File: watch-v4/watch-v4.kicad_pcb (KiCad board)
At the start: 4 copper layers, 35 x 35 mm, 35 parts, among them J1 CONN_10, P1 array connection, Q1 MOSFET_P, SW1 SPST, SW2 SPST, SW3 SPST, U1 IC_MCP73831, U2 MAX1722, U3 DS3231, U4 LSM9DS0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

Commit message: up to version 5.2
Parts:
- removed P1: array connection, watch-v4:Pin_Header_Straight_1x02
- added R4: 10kΩ, Resistors_SMD:R_0603, F.Cu at (159.3, 114.7)
- added R7: 10kΩ, Resistors_SMD:R_0603, F.Cu at (173.1, 114.2)
- added R8: 10kΩ, Resistors_SMD:R_0603, F.Cu at (176.0, 114.2)
- SW1, SW2, SW3: footprint watch-v4:panasonic-evpav-switch -> watch-v4:SW_Tactile_SPST_Angled_no_anchors
- moved C8 31.9 mm to (162.3, 113.1)
- moved SW3 31.0 mm to (183.6, 114.2), turned to 180 degrees
- moved U6 30.4 mm to (176.9, 112.2)
- moved ANT1 30.1 mm to (181.5, 111.9)
- moved XL1 30.1 mm to (177.5, 83.3), turned to 180 degrees
- moved C13 26.9 mm to (169.8, 108.2)
- moved SW1 26.3 mm to (156.3, 114.2), turned to 180 degrees
- moved C14 25.5 mm to (169.8, 110.2)
- moved R1 23.8 mm to (183.8, 85.2), turned to 270 degrees
- moved D2 23.1 mm to (183.7, 82.3), turned to 90 degrees
- moved D1 21.9 mm to (174.7, 91.7)
- moved X1 20.9 mm to (184.1, 109.1), turned to 90 degrees
- moved C1 20.9 mm to (181.5, 88.3)
- moved U5 19.6 mm to (177.5, 107.3), turned to 270 degrees
- moved R3 19.5 mm to (183.8, 87.7)
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- renumbered 12pf1 to 12p
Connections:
- net Net-(SW1-Pad2) renamed /SW1
- net Net-(SW2-Pad2) renamed /SW2
- net Net-(SW3-Pad2) renamed /SW3
- U5 pad 10: DISPLAY_SS -> DISPLAY_SCK
- U5 pad 32: Net-(U5-Pad31) -> Net-(U5-Pad32)
- U5 pad 8: DISPLAY_SCK -> DISPLAY_SS
- U6 pad 1: Net-(U5-Pad31) -> Net-(ANT1-Pad1)
- U6 pad 3: Net-(ANT1-Pad1) -> Net-(U5-Pad32)
- U6 pad 4: Net-(ANT1-Pad1) -> Net-(U5-Pad31)
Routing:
- net VCC: track 133.9 -> 15.3 mm, vias 8 -> 2
- net GND: track 135.4 -> 88.3 mm, vias 5 -> 9
- net SDA: track 54.8 -> 10.4 mm, vias 4 -> 0
- net SCL: track 50.1 -> 8.90 mm, vias 4 -> 0
- net /SW3: track 52.4 -> 15.0 mm, vias 2 -> 0
- net /SW1: track 30.3 -> 0.00 mm, vias 2 -> 0
- net /SW2: track 39.3 -> 9.65 mm, vias 2 -> 0
- net /EXTVCC: track 48.4 -> 25.0 mm, vias 1 -> 0
- net DISPLAY_SS: track 17.0 -> 0.00 mm
- net DISPLAY_MOSI: track 15.6 -> 0.00 mm
- net DISPLAY_SCK: track 14.2 -> 0.00 mm
- net /Regulator_In: track 22.5 -> 31.7 mm, vias 2 -> 3
- net /RX: track 27.4 -> 19.6 mm
- net Net-(R2-Pad1): track 9.80 -> 3.00 mm
- net Net-(C5-Pad1): track 6.57 -> 0.00 mm
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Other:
- outline, holes or cut-outs redrawn
- board text added: "Ourglass Rev 4.6"
- board text removed: "Ourglass Rev 4.5"

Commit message: save v5.2
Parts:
- added U7: NeoPixel, LEDs:Neopixel, B.Cu at (175.4, 96.3)
- moved L1 0.48 mm to (174.1, 100.4), turned to 270 degrees
- moved 12p 0.37 mm to (183.3, 105.5)
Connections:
- U3 pad 3: Net-(U3-Pad3) -> /ClockINT
- U4 pad 13: Net-(U4-Pad13) -> /Accel_INT
- U5 pad 25: Net-(U5-Pad25) -> /Backlight
- U5 pad 47: Net-(U5-Pad47) -> /ClockINT
- U5 pad 48: Net-(U5-Pad48) -> /Accel_INT
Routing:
- net VCC: track 15.3 -> 92.6 mm, vias 2 -> 9
- net GND: track 88.3 -> 148.3 mm, vias 9 -> 16
- net /Accel_INT: track 0.00 -> 30.6 mm, vias 0 -> 2
- net /SW1: track 0.00 -> 29.3 mm
- net SDA: track 10.4 -> 33.9 mm, vias 0 -> 2
- net SCL: track 8.90 -> 31.6 mm, vias 0 -> 2
- net /Backlight: track 0.00 -> 22.1 mm, vias 0 -> 1
- net /ClockINT: track 0.00 -> 21.4 mm, vias 0 -> 2
- net Net-(C6-Pad1): track 0.00 -> 13.8 mm, vias 0 -> 2
- net Net-(C5-Pad1): track 0.00 -> 8.43 mm
- net /SW2: track 9.65 -> 17.7 mm
- net Net-(C5-Pad2): track 0.00 -> 7.42 mm
- net DISPLAY_SCK: track 0.00 -> 5.91 mm
- net DISPLAY_MOSI: track 0.00 -> 5.17 mm
- net /Reset: track 27.5 -> 32.1 mm
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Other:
- board text added: "Ourglass Rev 5.2"
- board text removed: "Ourglass Rev 4.6"

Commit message: further v6 work; incomplete
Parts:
- removed 12p: C9, Capacitors_SMD:C_0603
- removed SW1, SW2, SW3: SPST, watch-v4:SW_Tactile_SPST_Angled_no_anchors
- removed U7: NeoPixel, LEDs:Neopixel
- added 12pf1: C9, Capacitors_SMD:C_0603, F.Cu at (183.4, 105.7)
- added C11: 2n2, Capacitors_SMD:C_0603, F.Cu at (180.1, 112.2)
- added C12: 1u, Capacitors_SMD:C_0603, B.Cu at (180.2, 85.2)
- added C4: 100n, Capacitors_SMD:C_0603, F.Cu at (183.2, 110.8)
- added C9: 47n, Capacitors_SMD:C_0603, F.Cu at (174.2, 114.1)
- added D3: LED, Capacitors_SMD:C_0603, B.Cu at (174.2, 106.5)
- added D4: LED, Capacitors_SMD:C_0603, B.Cu at (174.5, 97.6)
- added D5: LED, Capacitors_SMD:C_0603, B.Cu at (173.9, 87.8)
- added P1: Expansion Header, Socket_Strips:Socket_Strip_Straight_1x12_small, F.Cu at (172.1, 103.8)
- added Q2: BSS138, TO_SOT_Packages_SMD:SOT-23, B.Cu at (178.6, 95.3)
- added R9: 47, Resistors_SMD:R_0603, B.Cu at (173.9, 113.7)
- C1, C2, C5, C6, C7, C8, D1, Q1, R5, R6, U1, U2, U3, U4: moved to B.Cu
- C13: value 0.1uf -> 0u1; moved to B.Cu
- C14: value 0.1uf -> 1nf; moved to B.Cu
- C3: value 4.7uf -> 4u7; moved to B.Cu
- D2: footprint LED-0603 -> Capacitors_SMD:C_0603
- LIPOLY1: footprint watch-v4:Pin_Header_Straight_1x02 -> Socket_Strips:molex_2_pos
- R1: value 47Ω -> 47
- R2, R4: value 10kΩ -> 10k; moved to B.Cu
- R3: value R100kΩ -> 100k; moved to B.Cu
- R7, R8: value 10kΩ -> 10M; moved to B.Cu
- moved R7 33.0 mm to (179.7, 81.8)
- moved R8 31.0 mm to (179.8, 83.5)
- moved U4 28.9 mm to (181.8, 112.2), turned to 90 degrees
- moved R4 27.3 mm to (181.4, 98.7)
- moved C14 21.5 mm to (183.3, 93.5), turned to 0 degrees
- moved R5 20.6 mm to (177.8, 107.6), turned to 270 degrees
- moved U3 19.5 mm to (181.4, 103.7), turned to 0 degrees
- moved R6 18.9 mm to (176.0, 107.5), turned to 270 degrees
- moved C13 18.9 mm to (183.3, 95.1), turned to 0 degrees
- moved C7 18.5 mm to (175.8, 110.5), turned to 90 degrees
- moved C5 16.4 mm to (175.8, 113.6), turned to 270 degrees
- moved C8 15.5 mm to (177.6, 110.5), turned to 90 degrees
- moved C6 15.4 mm to (177.6, 113.6), turned to 270 degrees
- moved L1 13.1 mm to (180.5, 88.9)
- moved R3 11.6 mm to (173.5, 82.4), turned to 90 degrees
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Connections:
- net DISPLAY_MOSI renamed /Display_MOSI
- net DISPLAY_SCK renamed /Display_SCK
- net DISPLAY_SS renamed /Display_SS
- net Net-(12pf1-Pad2) renamed /XC2
- net Net-(C10-Pad1) renamed /XC1
- net Net-(U5-Pad31) renamed /Bal1
- net Net-(U5-Pad32) renamed /Bal2
- C13 pad 2: VCC -> /VCC
- C14 pad 2: VCC -> /VCC
- C7 pad 1: VCC -> /VCC
- C8 pad 1: VCC -> /VCC
- J1 pad 5: VCC -> /VCC
- J1 pad 6: VCC -> /VCC
- J1 pad 7: VCC -> /VCC
- J1 pad 8: VCC -> /VCC
- R4 pad 1: /SW1 -> /VCC
- R4 pad 2: GND -> /ClockINT
- R5 pad 1: SDA -> /SCL
- R5 pad 2: VCC -> /VCC
- R6 pad 1: SCL -> /SDA
- R6 pad 2: VCC -> /VCC
- R7 pad 1: /SW2 -> /VBAT
- R7 pad 2: GND -> /BatterySense
- R8 pad 1: GND -> /BatterySense
- R8 pad 2: /SW3 -> GND
- U2 pad 4: VCC -> /VCC
- U3 pad 2: VCC -> /VCC
- U3 pad 6: VCC -> /VCC
- U3 pad 7: SDA -> /SCL
- U3 pad 8: SCL -> /SDA
- U4 pad 15: VCC -> /VCC
- U4 pad 16: VCC -> /VCC
- U4 pad 17: VCC -> /VCC
- U4 pad 18: VCC -> /VCC
- U4 pad 19: VCC -> /VCC
- U4 pad 20: VCC -> /VCC
- U4 pad 21: SCL -> /SCL
- U4 pad 24: SDA -> /SDA
- U5 pad 1: VCC -> /VCC
- U5 pad 12: VCC -> /VCC
- U5 pad 14: /SW1 -> /EX8
- U5 pad 15: /SW2 -> /EX9
- U5 pad 16: /SW3 -> /EX10
- U5 pad 17: Net-(U5-Pad17) -> /EX11
- U5 pad 18: Net-(U5-Pad18) -> /EX12
- U5 pad 19: Net-(U5-Pad19) -> /EX13
- U5 pad 20: Net-(U5-Pad20) -> /EX14
- U5 pad 21: Net-(U5-Pad21) -> /EX15
- U5 pad 22: Net-(U5-Pad22) -> /BatterySense
- U5 pad 30: Net-(U5-Pad30) -> /VDD_PA
- U5 pad 35: VCC -> /VCC
- U5 pad 36: VCC -> /VCC
- U5 pad 6: SCL -> /SCL
- U5 pad 7: SDA -> /SDA
- U6 pad 5: GND -> /VDD_PA
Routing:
- net GND: track 148.3 -> 0.00 mm, vias 16 -> 0
- net VCC: track 92.6 -> 0.00 mm, vias 9 -> 0
- net SDA: track 33.9 -> 0.00 mm, vias 2 -> 0
- net /Reset: track 32.1 -> 0.00 mm, vias 2 -> 0
- net SCL: track 31.6 -> 0.00 mm, vias 2 -> 0
- net /Accel_INT: track 30.6 -> 0.00 mm, vias 2 -> 0
- net /SW1: track 29.3 -> 0.00 mm
- net /EXTVCC: track 25.0 -> 0.00 mm
- net /Regulator_In: track 28.0 -> 3.61 mm, vias 3 -> 0
- net /VBAT: track 24.0 -> 0.00 mm, vias 1 -> 0
- net /Backlight: track 22.1 -> 0.00 mm, vias 1 -> 0
- net /TX: track 22.0 -> 0.00 mm, vias 2 -> 0
- net /ClockINT: track 21.4 -> 0.00 mm, vias 2 -> 0
- net /RX: track 19.5 -> 0.00 mm, vias 2 -> 0
- net /SW2: track 17.7 -> 0.00 mm
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- removed copper zone on B.Cu, net GND
- removed copper zone on F.Cu, net GND
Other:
- board size 35 x 35 mm -> 13 x 35 mm
- board text added: "Ourglass Rev 6.0"
- board text removed: "Ourglass Rev 5.2"

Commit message: further traces routed, still more work to go
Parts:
- C13: value 0u1 -> 0.1uf
- C3: value 4u7 -> 4.7uf
- R1: value 47 -> 47Ω
- R2: value 10k -> 10kΩ
- R3: value 100k -> R100kΩ
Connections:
- P1 pad 1: /VCC -> GND
- P1 pad 2: GND -> /VCC
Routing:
- net GND: track 0.00 -> 41.1 mm, vias 0 -> 7
- net /EXTVCC: track 0.00 -> 21.5 mm, vias 0 -> 3
- net /Regulator_In: track 3.61 -> 22.8 mm, vias 0 -> 1
- net /VBAT: track 0.00 -> 13.3 mm, vias 0 -> 1
- net Net-(D2-Pad2): track 0.00 -> 3.81 mm
- net /BatterySense: track 0.00 -> 3.58 mm
- net /VCC: track 0.00 -> 3.31 mm
- net Net-(L1-Pad2): track 0.00 -> 2.96 mm, vias 0 -> 1
- net Net-(D2-Pad1): track 0.00 -> 2.10 mm, vias 0 -> 1
- net Net-(R2-Pad1): track 0.00 -> 1.80 mm

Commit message: further traces routed, still more work to go
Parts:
- C10: value 12pf -> 12p
- C5: value .22uf -> u22
- C6: value 4.7uf -> 4u7
- C8: value 0.1uf -> u1
- turned D1 to 180 degrees
- renumbered 12pf1 to 12p
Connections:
- P1 pad 3: /SDA -> /SCL
- P1 pad 4: /SCL -> /SDA
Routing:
- net /EXTVCC: track 21.5 -> 35.4 mm, vias 3 -> 2
- net /Regulator_In: track 22.8 -> 18.0 mm
- net /EX8: track 0.00 -> 4.78 mm
- net GND: track 41.1 -> 45.8 mm
- net /EX15: track 0.00 -> 4.57 mm
- net /EX9: track 0.00 -> 3.95 mm
- net /EX14: track 0.00 -> 3.86 mm
- net /EX13: track 0.00 -> 2.97 mm
- net /EX10: track 0.00 -> 2.89 mm
- net /EX12: track 0.00 -> 2.61 mm
- net /EX11: track 0.00 -> 2.53 mm
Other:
- board text added: "10"
- board text added: "11"
- board text added: "12"
- board text added: "13"
- board text added: "14"
- board text added: "15"
- board text added: "8"
- board text added: "9"
- board text added: "GND"
- board text added: "SCL"
- board text added: "SDA"
- board text added: "VCC"

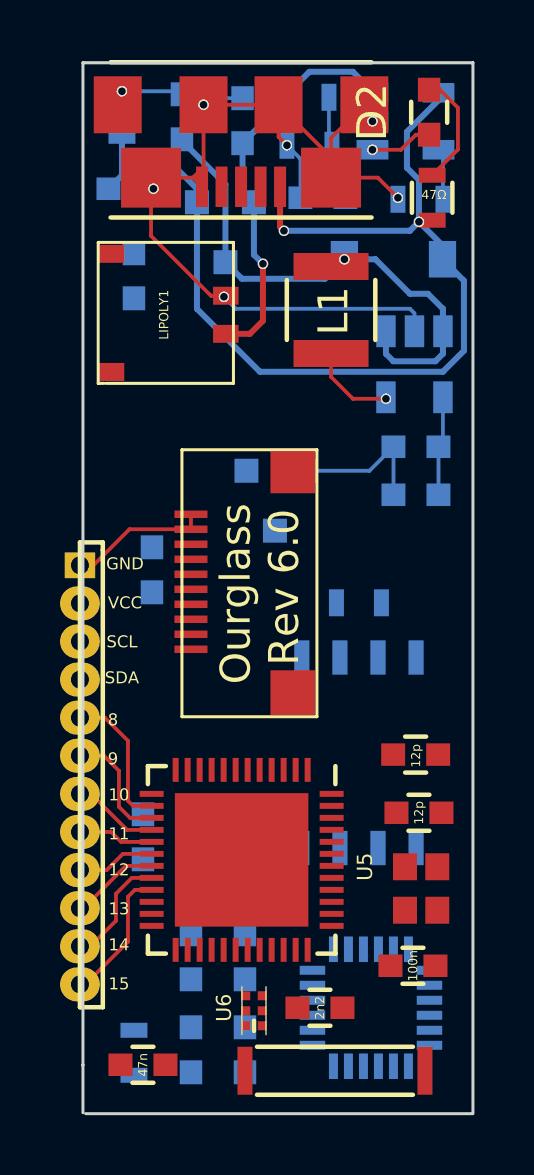
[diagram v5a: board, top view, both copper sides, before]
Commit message: top layer components mostly routed
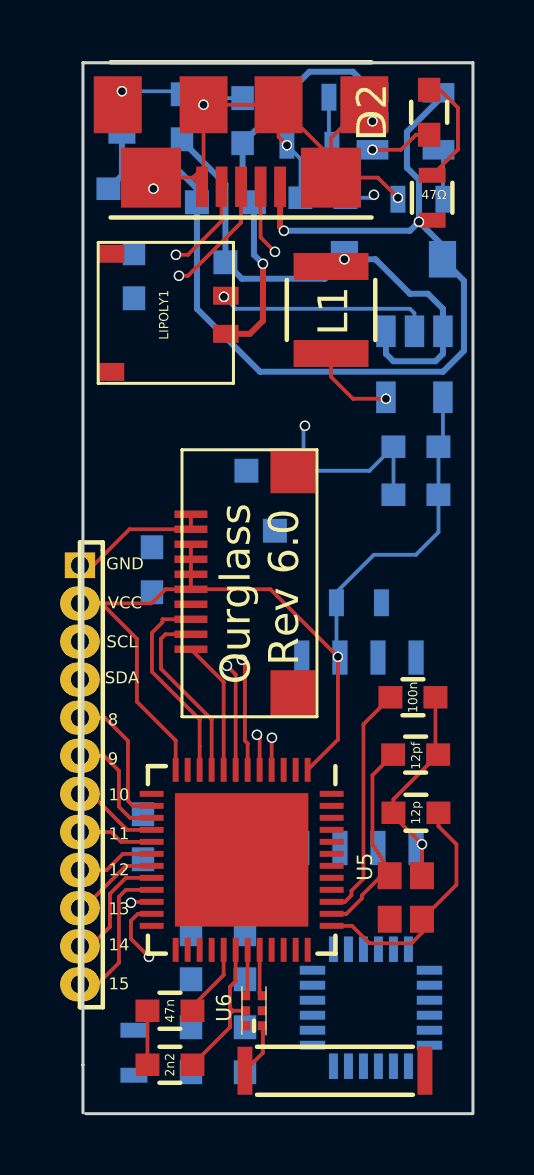
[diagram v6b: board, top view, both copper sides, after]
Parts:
- C10: value 12p -> 12pf
- C5: value u22 -> .22uf
- C6: value 4u7 -> 4.7uf
- C8: value u1 -> 0.1uf
- moved C4 8.95 mm to (183.2, 101.8)
- moved C11 5.35 mm to (175.1, 114.1)
- moved C9 2.01 mm to (175.1, 112.3), turned to 180 degrees
- moved X1 0.59 mm to (183.6, 109.4)
- moved 12p 0.10 mm to (183.3, 105.7)
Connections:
- XL1 pad 2: /RX -> /TX
- XL1 pad 3: /TX -> /RX
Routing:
- net /BatterySense: track 3.58 -> 41.1 mm, vias 0 -> 2
- net /VCC: track 3.31 -> 33.7 mm, vias 0 -> 1
- net /Reset: track 0.00 -> 29.1 mm, vias 0 -> 2
- net /RX: track 0.00 -> 21.6 mm, vias 0 -> 2
- net GND: track 45.8 -> 67.2 mm, vias 7 -> 9
- net /TX: track 0.00 -> 19.7 mm, vias 0 -> 2
- net /SCL: track 0.00 -> 9.40 mm, vias 0 -> 1
- net /SDA: track 0.00 -> 8.68 mm, vias 0 -> 1
- net /XC2: track 0.00 -> 8.12 mm
- net Net-(C4-Pad1): track 0.00 -> 7.89 mm
- net /XC1: track 0.00 -> 7.54 mm
- net /Display_SCK: track 0.00 -> 6.77 mm
- net /Display_MOSI: track 0.00 -> 6.13 mm
- net /VDD_PA: track 0.00 -> 5.13 mm
- net /Display_SS: track 0.00 -> 4.47 mm
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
